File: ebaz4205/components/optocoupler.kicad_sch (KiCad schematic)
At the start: 1 part

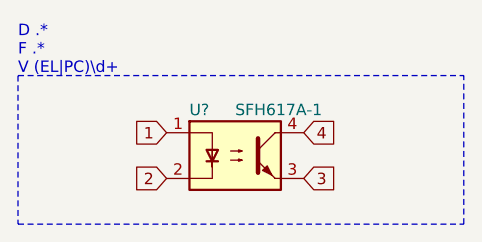
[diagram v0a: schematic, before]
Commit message: Consolidated all custom symbols into single library.
Library is available at ebaz4205/components/ebaz4205.kicad_sym

The templates and the schematics have been updated to use this library.
Keeping the original libraries for future reference.
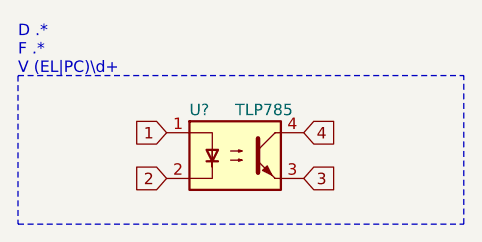
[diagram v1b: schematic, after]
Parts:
- removed U?: SFH617A-1, Package_DIP:DIP-4_W7.62mm, symbol Isolator:SFH617A-1
- added U?: TLP785, Package_DIP:DIP-4_W7.62mm, symbol ebaz4205:TLP785
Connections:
- net 1: now also U?.1
- net 2: now also U?.2
- net 3: now also U?.3
- net 4: now also U?.4
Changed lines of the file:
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@@
     (effects (font (size 1.27 1.27)) (justify left))
   )
-  (symbol (lib_id "Isolator:SFH617A-1") (at 24.13 8.89 0) (unit 1)
+  (symbol (lib_id "ebaz4205:TLP785") (at 24.13 8.89 0) (unit 1)
     (in_bom yes) (on_board yes)
     (property "Reference" "U?" (id 0) (at 19.05 3.81 0)
       (effects (font (size 1.27 1.27)) (justify left))
     )
-    (property "Value" "SFH617A-1" (id 1) (at 24.13 3.81 0)
+    (property "Value" "TLP785" (id 1) (at 24.13 3.81 0)
       (effects (font (size 1.27 1.27)) (justify left))
     )
@@
       (effects (font (size 1.27 1.27) italic) (justify left) hide)
     )
-    (property "Datasheet" "http://www.vishay.com/docs/83740/sfh617a.pdf" (id 3) (at 24.13 8.89 0)
+    (property "Datasheet" "https://toshiba.semicon-storage.com/info/docget.jsp?did=10569&prodName=TLP785" (id 3) (at 24.13 8.89 0)
       (effects (font (size 1.27 1.27)) (justify left) hide)
     )
@@
   )
   (symbol_instances
-    (path "/787a1171-deee-4184-a01d-ec7b1313eeac"
-      (reference "U?") (unit 1) (value "SFH617A-1") (footprint "Package_DIP:DIP-4_W7.62mm")
+    (path "/c03a07cb-93b2-4bb7-9251-39f63979633d"
+      (reference "U?") (unit 1) (value "TLP785") (footprint "Package_DIP:DIP-4_W7.62mm")
     )
   )
